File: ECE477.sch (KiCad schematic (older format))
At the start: 44 parts, among them IC1 LP3852EMP-3.3_NOPB, IC5 BQ29330DBT, J1 P7805-2000-S, U1 STM32H7_LQFP144_T2

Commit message: Adding NRST + Boot
Added NRST + Boot
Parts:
- added C?: .1uF, Capacitor_SMD:C_0805_2012Metric_Pad1.15x1.40mm_HandSolder, symbol pspice:CAP
- added R? (x2): 100k, Resistor_SMD:R_0805_2012Metric_Pad1.15x1.40mm_HandSolder, symbol Device:R_US
- added SW?: SW_Push_Dual, symbol Switch:SW_Push_Dual
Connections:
- net GND: now also C?.2, R?.1, SW?.3, SW?.4
- net VBAT: now also R?.2
- net BOOT0: now reaches U1.135 (BOOT0)
- net BOOT0: now also R?.2
- net NRST: now reaches U1.27 (NRST)
- net NRST: now also C?.1, R?.1, SW?.1, SW?.2
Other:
- note added: "Two more USART 1 - 2 - 3 \n4 x PWM -- servo one GPIO \nLEDs \nPWR swtch\nmake sure GPIO are ocnnected to advanced timers\n\n\n\n"
- note removed: "Two more USART 1 - 2 - 3 \n4 x PWM -- servo one GPIO \nLEDs \nPWR swtch + reset button\nmake sure GPIO are ocnnected to advanced timers\n\n\n\n"
- moved on the sheet: U1B
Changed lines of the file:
@@
 L ECE477-rescue:STM32H7_LQFP144_T2-2020-08-25_13-35-24 U1
 U 2 1 5F46EB3B
-P 25800 2250
-F 0 "U1" H 26900 2637 60  0000 C CNN
-F 1 "STM32H7_LQFP144_T2" H 26900 2531 60  0000 C CNN
-F 2 "STM_footprints:STM32H7_LQFP144_T2" H 27000 2490 60  0001 C CNN
-F 3 "" H 25800 2250 60  0000 C CNN
-	2    25800 2250
+P 19550 2150
+F 0 "U1" H 20650 2537 60  0000 C CNN
+F 1 "STM32H7_LQFP144_T2" H 20650 2431 60  0000 C CNN
+F 2 "STM_footprints:STM32H7_LQFP144_T2" H 20750 2390 60  0001 C CNN
+F 3 "" H 19550 2150 60  0000 C CNN
+	2    19550 2150
 	1    0    0    -1
 $EndComp
@@
 	14800 4600 15150 4600
 Text Notes 14950 7200 0    50   ~ 0
-Two more USART 1 - 2 - 3 \n4 x PWM -- servo one GPIO \nLEDs \nPWR swtch + reset button\nmake sure GPIO are ocnnected to advanced timers\n\n\n\n
+Two more USART 1 - 2 - 3 \n4 x PWM -- servo one GPIO \nLEDs \nPWR swtch\nmake sure GPIO are ocnnected to advanced timers\n\n\n\n
+$Comp
+L Switch:SW_Push_Dual SW?
+U 1 1 5F877F07
+P 5850 13350
+F 0 "SW?" H 5850 13635 50  0000 C CNN
+F 1 "SW_Push_Dual" H 5850 13544 50  0000 C CNN
+F 2 "" H 5850 13550 50  0001 C CNN
+F 3 "~" H 5850 13550 50  0001 C CNN
+	1    5850 13350
+	1    0    0    -1
+$EndComp
+$Comp
+L pspice:CAP C?
+U 1 1 5F887729
+P 6600 13450
+F 0 "C?" H 6778 13496 50  0000 L CNN
+F 1 ".1uF" H 6778 13405 50  0000 L CNN
+F 2 "Capacitor_SMD:C_0805_2012Metric_Pad1.15x1.40mm_HandSolder" H 6600 13450 50  0001 C CNN
+F 3 "~" H 6600 13450 50  0001 C CNN
+	1    6600 13450
+	1    0    0    -1
+$EndComp
+$Comp
+L Device:R_US R?
+U 1 1 5F8954D3
+P 5850 12600
+F 0 "R?" H 5918 12646 50  0000 L CNN
+F 1 "100k" H 5918 12555 50  0000 L CNN
+F 2 "Resistor_SMD:R_0805_2012Metric_Pad1.15x1.40mm_HandSolder" V 5890 12590 50  0001 C CNN
+F 3 "~" H 5850 12600 50  0001 C CNN
+	1    5850 12600
+	-1   0    0    1
+$EndComp
+Wire Wire Line
+	6600 13200 6600 12900
+Wire Wire Line
+	6600 12900 5850 12900
+Connection ~ 5850 12900
+Wire Wire Line
+	5850 12900 5850 12750
+Wire Wire Line
+	5850 12300 5850 12450
+Wire Wire Line
+	5650 13550 5850 13550
+Wire Wire Line
+	5850 13550 5850 13750
+Connection ~ 5850 13550
+Wire Wire Line
+	5850 13550 6050 13550
+Wire Wire Line
+	5650 13350 5850 13350
+Wire Wire Line
+	5850 12900 5850 13350
+Connection ~ 5850 13350
+Wire Wire Line
+	5850 13350 6050 13350
+Wire Wire Line
+	6600 13700 6600 13750
+Wire Wire Line
+	6600 13750 5850 13750
+Connection ~ 5850 13750
+Wire Wire Line
+	5850 13750 5850 13900
+Wire Wire Line
+	6600 12900 6800 12900
+Connection ~ 6600 12900
+Text GLabel 6800 12900 2    50   Input ~ 0
+NRST
+Text GLabel 5850 12300 1    50   Input ~ 0
+VDD_MCU
+$Comp
+L power:GND #PWR?
+U 1 1 5F9369F7
+P 5850 13900
+F 0 "#PWR?" H 5850 13650 50  0001 C CNN
+F 1 "GND" H 5855 13727 50  0000 C CNN
+F 2 "" H 5850 13900 50  0001 C CNN
+F 3 "" H 5850 13900 50  0001 C CNN
+	1    5850 13900
+	1    0    0    -1
+$EndComp
+Wire Wire Line
+	21750 3450 22000 3450
+Text GLabel 22000 3450 2    50   Input ~ 0
+NRST
+$Comp
+L Device:R_US R?
+U 1 1 5F993DC3
+P 22300 3750
+F 0 "R?" H 22368 3796 50  0000 L CNN
+F 1 "100k" H 22368 3705 50  0000 L CNN
+F 2 "Resistor_SMD:R_0805_2012Metric_Pad1.15x1.40mm_HandSolder" V 22340 3740 50  0001 C CNN
+F 3 "~" H 22300 3750 50  0001 C CNN
+	1    22300 3750
+	0    1    1    0
+$EndComp
+Wire Wire Line
+	21750 3650 22050 3650
+Wire Wire Line
+	22050 3650 22050 3750
+Wire Wire Line
+	22050 3750 22150 3750
+Wire Wire Line
+	22450 3750 22650 3750
+Connection ~ 22050 3650
+Wire Wire Line
+	22050 3650 22650 3650
+Text GLabel 22650 3650 2    50   Input ~ 0
+BOOT0
+$Comp
+L power:GND #PWR?
+U 1 1 5F9EC431
+P 22650 3750
+F 0 "#PWR?" H 22650 3500 50  0001 C CNN
+F 1 "GND" H 22655 3577 50  0000 C CNN
+F 2 "" H 22650 3750 50  0001 C CNN
+F 3 "" H 22650 3750 50  0001 C CNN
+	1    22650 3750
+	1    0    0    -1
+$EndComp
 $EndSCHEMATC

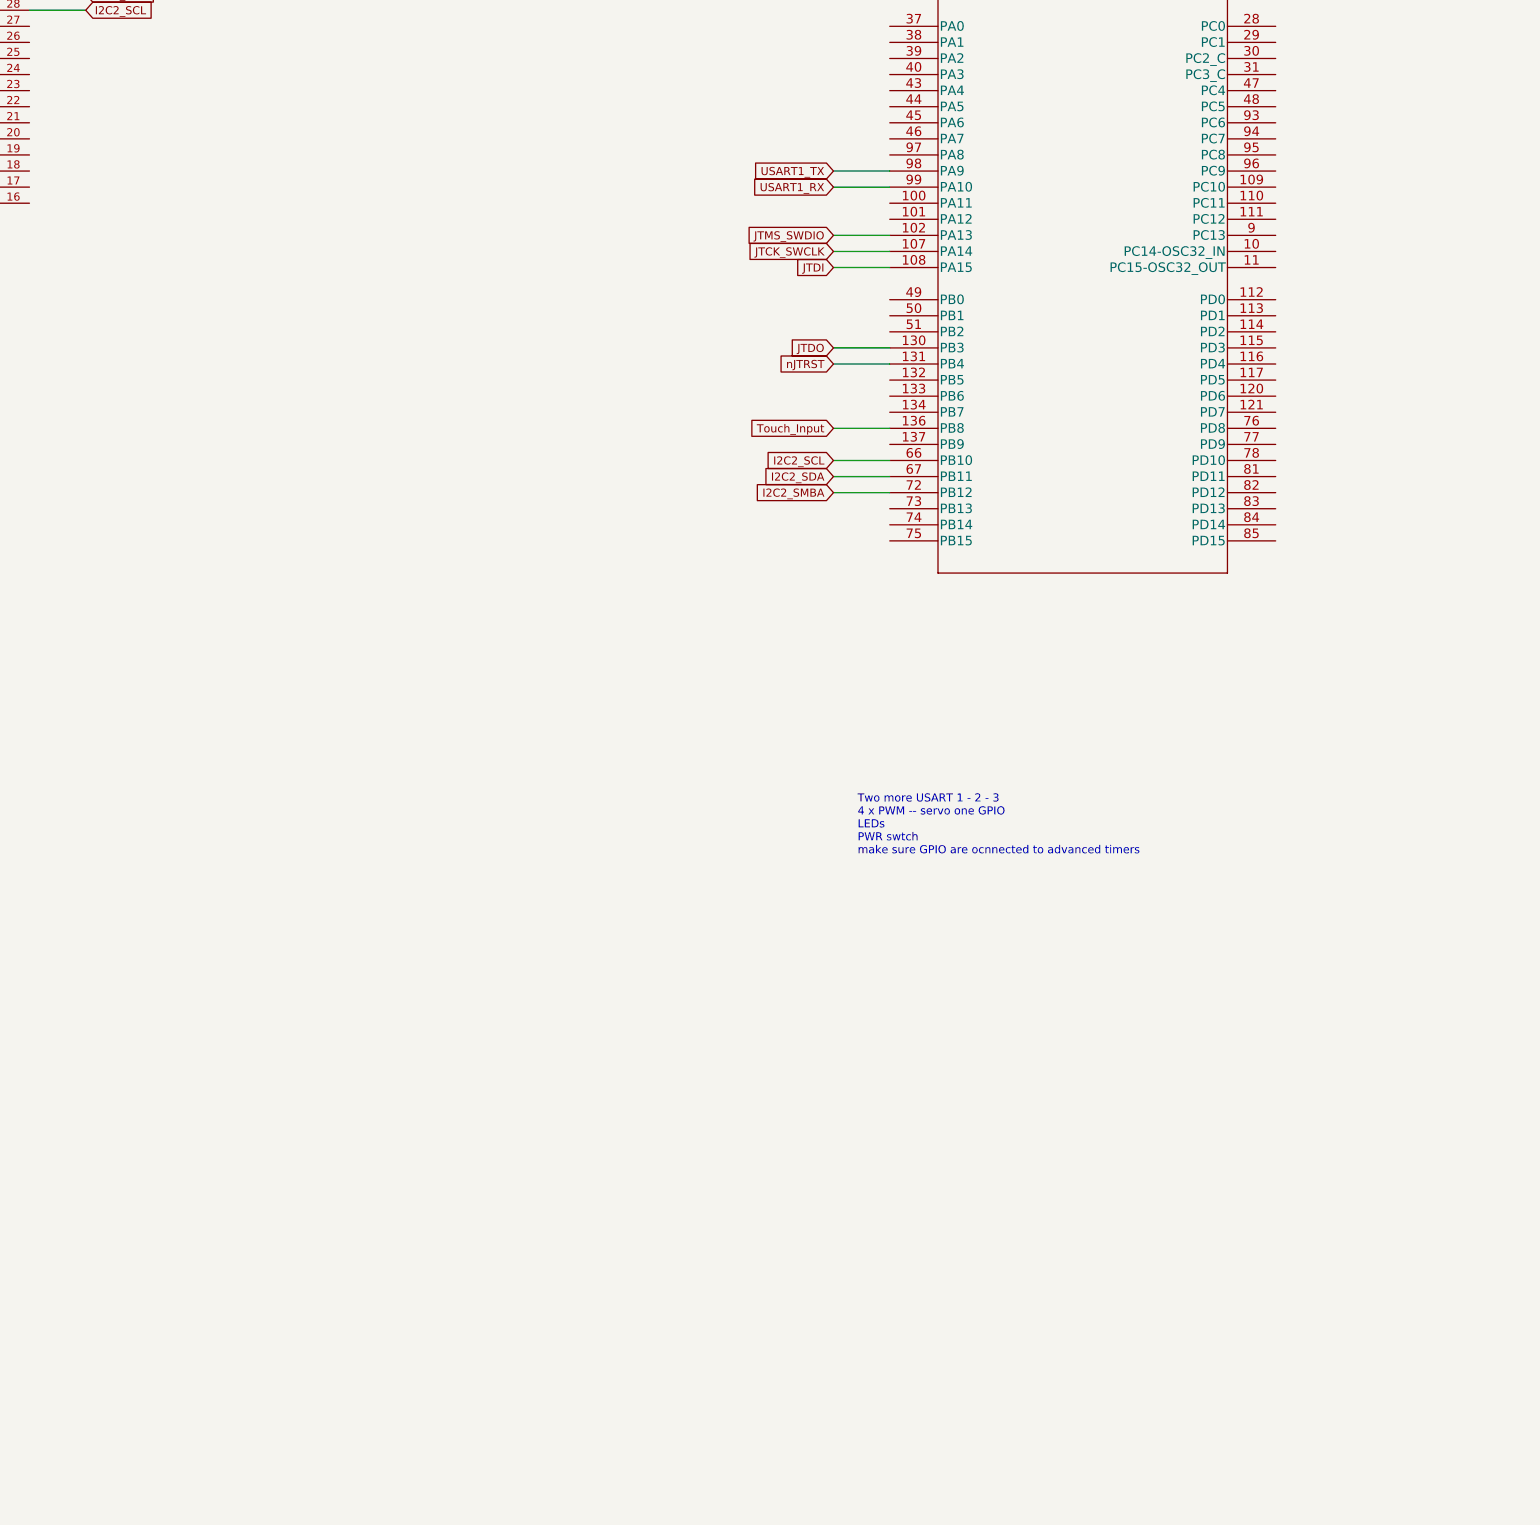
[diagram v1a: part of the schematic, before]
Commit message: Pinouts
Pin outs for USART GPIO and JTAG
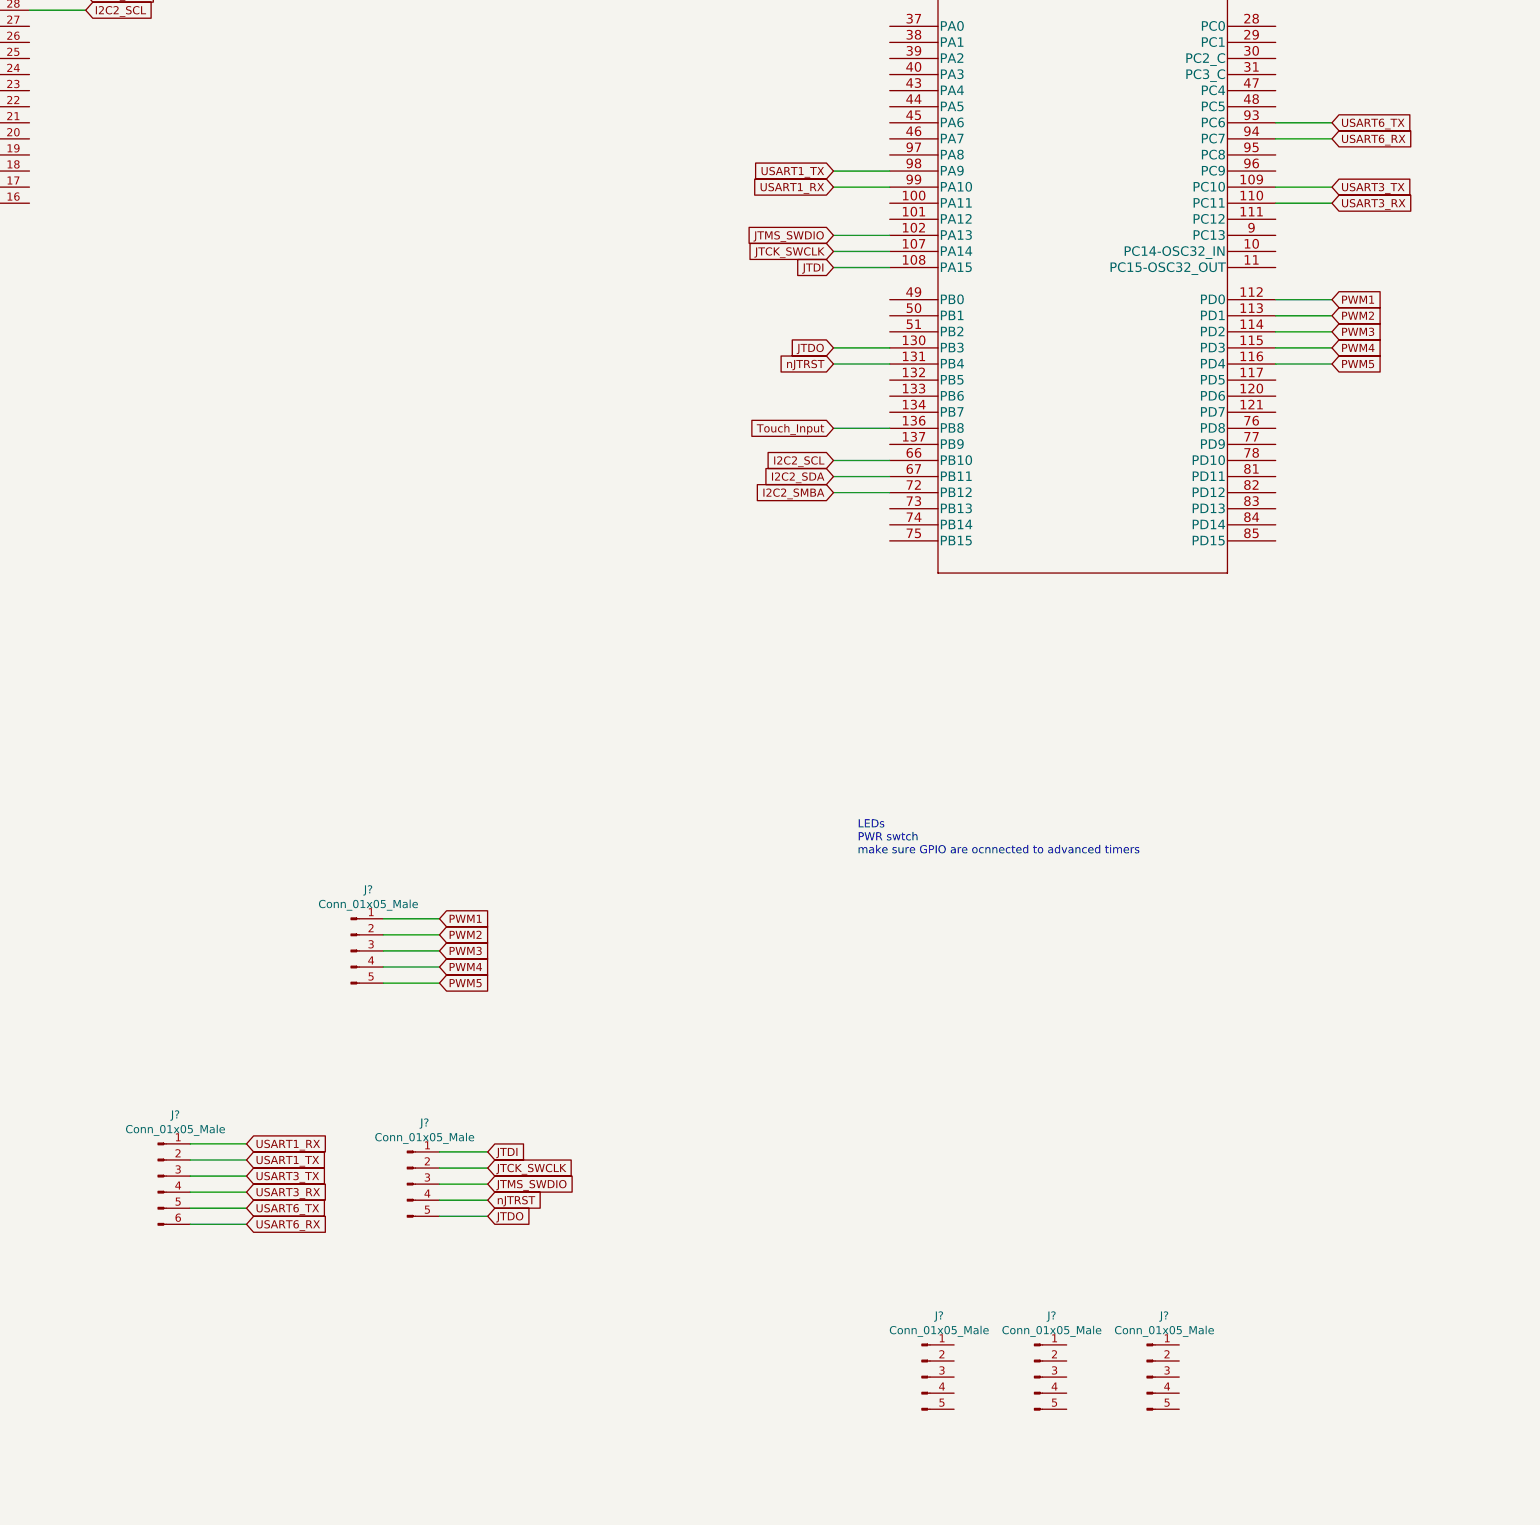
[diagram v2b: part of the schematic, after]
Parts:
- added J?: Conn_01x05_Male, symbol Connector:Conn_01x06_Male
- added J? (x5): Conn_01x05_Male, symbol Connector:Conn_01x05_Male
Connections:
- net JTCK_SWCLK: now also J?.2 (Pin_2)
- net JTDI: now also J?.1 (Pin_1)
- net JTDO: now also J?.5 (Pin_5)
- net JTMS_SWDIO: now also J?.3 (Pin_3)
- net USART1_RX: now also J?.1 (Pin_1)
- net USART1_TX: now also J?.2 (Pin_2)
- net nJTRST: now also J?.4 (Pin_4)
- net USART3_TX: now reaches U1.109 (PC10)
- net USART3_TX: now also J?.3 (Pin_3)
- net USART3_RX: now reaches U1.110 (PC11)
- net USART3_RX: now also J?.4 (Pin_4)
- net PWM1: now reaches U1.112 (PD0)
- net PWM1: now also J?.1 (Pin_1)
- net PWM2: now reaches U1.113 (PD1)
- net PWM2: now also J?.2 (Pin_2)
- net PWM3: now reaches U1.114 (PD2)
- net PWM3: now also J?.3 (Pin_3)
- net PWM4: now reaches U1.115 (PD3)
- net PWM4: now also J?.4 (Pin_4)
- net PWM5: now reaches U1.116 (PD4)
- net PWM5: now also J?.5 (Pin_5)
- net USART6_TX: now reaches U1.93 (PC6)
- net USART6_TX: now also J?.5 (Pin_5)
- net USART6_RX: now reaches U1.94 (PC7)
- net USART6_RX: now also J?.6 (Pin_6)
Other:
- note added: "LEDs \nPWR swtch\nmake sure GPIO are ocnnected to advanced timers\n\n\n\n"
- note removed: "Two more USART 1 - 2 - 3 \n4 x PWM -- servo one GPIO \nLEDs \nPWR swtch\nmake sure GPIO are ocnnected to advanced timers\n\n\n\n"
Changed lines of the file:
@@
 	14800 4600 15150 4600
 Text Notes 14950 7200 0    50   ~ 0
-Two more USART 1 - 2 - 3 \n4 x PWM -- servo one GPIO \nLEDs \nPWR swtch\nmake sure GPIO are ocnnected to advanced timers\n\n\n\n
+LEDs \nPWR swtch\nmake sure GPIO are ocnnected to advanced timers\n\n\n\n
 $Comp
 L Switch:SW_Push_Dual SW?
@@
 	1    0    0    -1
 $EndComp
+$Comp
+L Connector:Conn_01x06_Male J?
+U 1 1 5FA28754
+P 10600 8950
+F 0 "J?" H 10708 9331 50  0000 C CNN
+F 1 "Conn_01x05_Male" H 10708 9240 50  0000 C CNN
+F 2 "" H 10600 8950 50  0001 C CNN
+F 3 "~" H 10600 8950 50  0001 C CNN
+	1    10600 8950
+	1    0    0    -1
+$EndComp
+$Comp
+L Connector:Conn_01x05_Male J?
+U 1 1 5FA2B098
+P 12150 9000
+F 0 "J?" H 12258 9381 50  0000 C CNN
+F 1 "Conn_01x05_Male" H 12258 9290 50  0000 C CNN
+F 2 "" H 12150 9000 50  0001 C CNN
+F 3 "~" H 12150 9000 50  0001 C CNN
+	1    12150 9000
+	1    0    0    -1
+$EndComp
+$Comp
+L Connector:Conn_01x05_Male J?
+U 1 1 5FA398AC
+P 11800 7550
+F 0 "J?" H 11908 7931 50  0000 C CNN
+F 1 "Conn_01x05_Male" H 11908 7840 50  0000 C CNN
+F 2 "" H 11800 7550 50  0001 C CNN
+F 3 "~" H 11800 7550 50  0001 C CNN
+	1    11800 7550
+	1    0    0    -1
+$EndComp
+$Comp
+L Connector:Conn_01x05_Male J?
+U 1 1 5FA48124
+P 15350 10200
+F 0 "J?" H 15458 10581 50  0000 C CNN
+F 1 "Conn_01x05_Male" H 15458 10490 50  0000 C CNN
+F 2 "" H 15350 10200 50  0001 C CNN
+F 3 "~" H 15350 10200 50  0001 C CNN
+	1    15350 10200
+	1    0    0    -1
+$EndComp
+$Comp
+L Connector:Conn_01x05_Male J?
+U 1 1 5FA567D5
+P 16050 10200
+F 0 "J?" H 16158 10581 50  0000 C CNN
+F 1 "Conn_01x05_Male" H 16158 10490 50  0000 C CNN
+F 2 "" H 16050 10200 50  0001 C CNN
+F 3 "~" H 16050 10200 50  0001 C CNN
+	1    16050 10200
+	1    0    0    -1
+$EndComp
+$Comp
+L Connector:Conn_01x05_Male J?
+U 1 1 5FA64E72
+P 16750 10200
+F 0 "J?" H 16858 10581 50  0000 C CNN
+F 1 "Conn_01x05_Male" H 16858 10490 50  0000 C CNN
+F 2 "" H 16750 10200 50  0001 C CNN
+F 3 "~" H 16750 10200 50  0001 C CNN
+	1    16750 10200
+	1    0    0    -1
+$EndComp
+Wire Wire Line
+	17550 2400 17900 2400
+Wire Wire Line
+	17550 2500 17900 2500
+Text GLabel 17900 2400 2    50   Input ~ 0
+USART6_TX
+Text GLabel 17900 2500 2    50   Input ~ 0
+USART6_RX
+Wire Wire Line
+	17550 2800 17900 2800
+Wire Wire Line
+	17550 2900 17900 2900
+Text GLabel 17900 2800 2    50   Input ~ 0
+USART3_TX
+Text GLabel 17900 2900 2    50   Input ~ 0
+USART3_RX
+Wire Wire Line
+	10800 8750 11150 8750
+Wire Wire Line
+	10800 8850 11150 8850
+Wire Wire Line
+	10800 8950 11150 8950
+Wire Wire Line
+	10800 9050 11150 9050
+Wire Wire Line
+	10800 9150 11150 9150
+Wire Wire Line
+	10800 9250 11150 9250
+Text GLabel 11150 8850 2    50   Input ~ 0
+USART1_TX
+Text GLabel 11150 8750 2    50   Input ~ 0
+USART1_RX
+Text GLabel 11150 8950 2    50   Input ~ 0
+USART3_TX
+Text GLabel 11150 9050 2    50   Input ~ 0
+USART3_RX
+Text GLabel 11150 9150 2    50   Input ~ 0
+USART6_TX
+Text GLabel 11150 9250 2    50   Input ~ 0
+USART6_RX
+Wire Wire Line
+	12350 8800 12650 8800
+Wire Wire Line
+	12350 8900 12650 8900
+Wire Wire Line
+	12350 9000 12650 9000
+Wire Wire Line
+	12350 9100 12650 9100
+Wire Wire Line
+	12350 9200 12650 9200
+Text GLabel 12650 9000 2    50   Input ~ 0
+JTMS_SWDIO
+Text GLabel 12650 8900 2    50   Input ~ 0
+JTCK_SWCLK
+Text GLabel 12650 8800 2    50   Input ~ 0
+JTDI
+Text GLabel 12650 9200 2    50   Input ~ 0
+JTDO
+Text GLabel 12650 9100 2    50   Input ~ 0
+nJTRST
+Wire Wire Line
+	17550 3500 17900 3500
+Wire Wire Line
+	17550 3600 17900 3600
+Wire Wire Line
+	17550 3700 17900 3700
+Wire Wire Line
+	17550 3800 17900 3800
+Wire Wire Line
+	17550 3900 17900 3900
+Text GLabel 17900 3500 2    50   Input ~ 0
+PWM1
+Text GLabel 17900 3600 2    50   Input ~ 0
+PWM2
+Text GLabel 17900 3700 2    50   Input ~ 0
+PWM3
+Text GLabel 17900 3800 2    50   Input ~ 0
+PWM4
+Text GLabel 17900 3900 2    50   Input ~ 0
+PWM5
+Wire Wire Line
+	12000 7350 12350 7350
+Wire Wire Line
+	12000 7450 12350 7450
+Wire Wire Line
+	12000 7550 12350 7550
+Wire Wire Line
+	12000 7650 12350 7650
+Wire Wire Line
+	12000 7750 12350 7750
+Text GLabel 12350 7350 2    50   Input ~ 0
+PWM1
+Text GLabel 12350 7450 2    50   Input ~ 0
+PWM2
+Text GLabel 12350 7550 2    50   Input ~ 0
+PWM3
+Text GLabel 12350 7650 2    50   Input ~ 0
+PWM4
+Text GLabel 12350 7750 2    50   Input ~ 0
+PWM5
 $EndSCHEMATC
